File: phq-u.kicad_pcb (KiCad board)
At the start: 4 copper layers, 130.4 x 75.4 mm, 107 parts, among them J1 18…56 V, J2 MCU bypass, J3 Voltage select, J4 3.3…24 V, J5 MCU disable, J6 TC2030, J7 USB-C, J8 I/O, Q1 NX138AK, U1 i7A4W033A033V, U2 TMCS1108A1U, U3 TMCS1108A1U, U4 RPMH3.3-0.5, U5 ESP32-C3, U6 ECMF02-2AMX6

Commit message: Position mounting holes closer to corners
A distance of 7.5 mm to the edges should provide sufficient mechanical
stability.
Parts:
- moved H1 3.54 mm to (84.9, 69.7)
- moved H2 3.54 mm to (84.9, 130.1)
- moved H3 3.54 mm to (200.4, 69.7)
- moved H4 3.54 mm to (200.4, 130.1)
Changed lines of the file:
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@@
   )
   (footprint "MountingHole:MountingHole_3.2mm_M3_Pad_Via" (layer "F.Cu")
-    (at 87.44 72.2)
+    (at 84.94 69.7)
     (descr "Mounting Hole 3.2mm, M3")
     (tags "mounting hole 3.2mm m3")
@@
   )
   (footprint "MountingHole:MountingHole_3.2mm_M3_Pad_Via" (layer "F.Cu")
-    (at 197.87 72.2)
+    (at 200.37 69.7)
     (descr "Mounting Hole 3.2mm, M3")
     (tags "mounting hole 3.2mm m3")
@@
   )
   (footprint "MountingHole:MountingHole_3.2mm_M3_Pad_Via" (layer "F.Cu")
-    (at 197.87 127.6)
+    (at 200.37 130.1)
     (descr "Mounting Hole 3.2mm, M3")
     (tags "mounting hole 3.2mm m3")
@@
   )
   (footprint "MountingHole:MountingHole_3.2mm_M3_Pad_Via" (layer "F.Cu")
-    (at 87.44 127.6)
+    (at 84.94 130.1)
     (descr "Mounting Hole 3.2mm, M3")
     (tags "mounting hole 3.2mm m3")

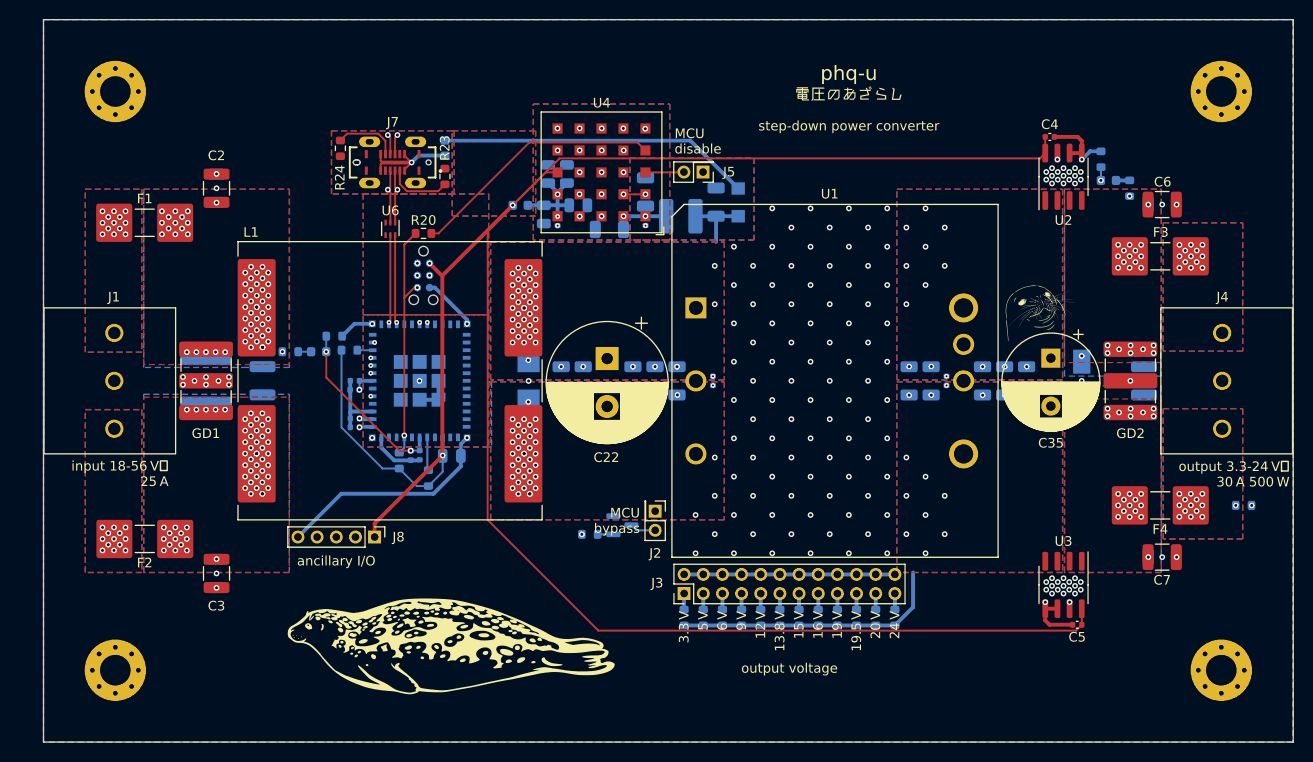
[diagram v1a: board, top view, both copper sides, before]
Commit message: Add 3.3 V TVS diodes and revise ground zones
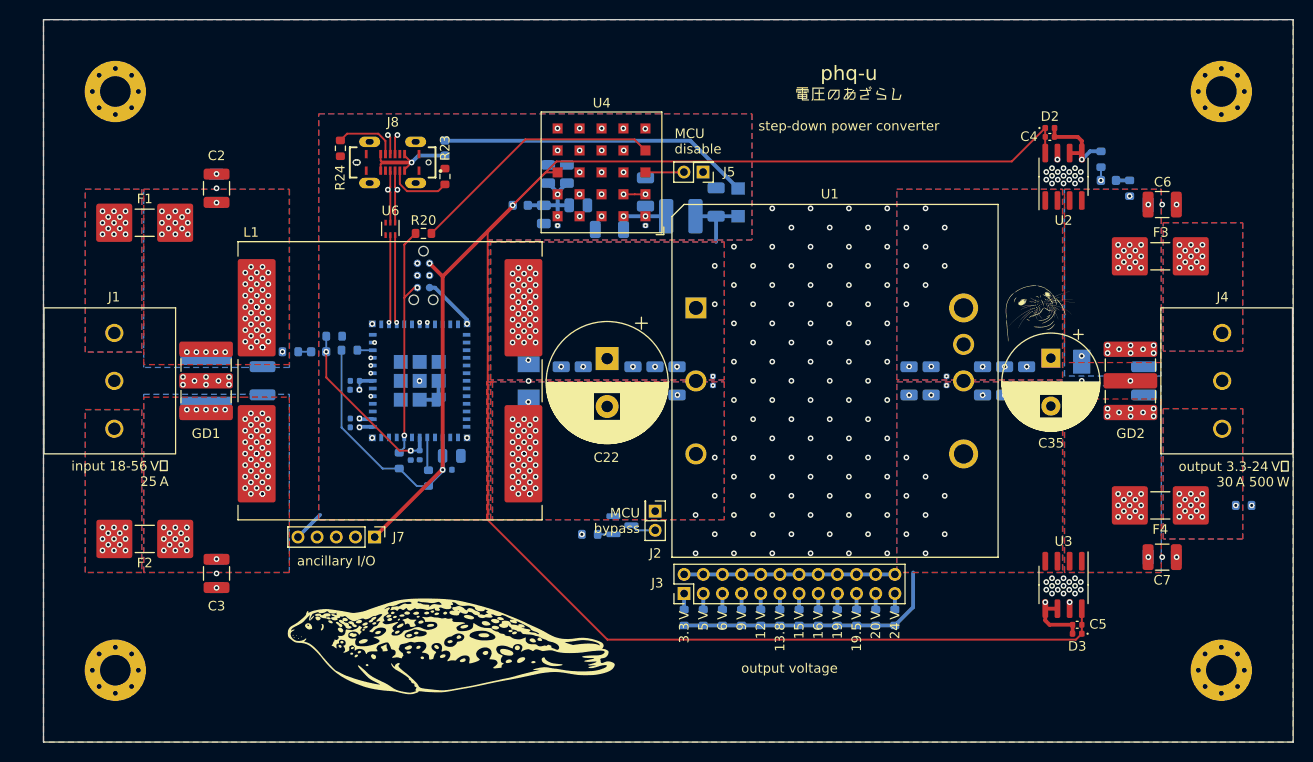
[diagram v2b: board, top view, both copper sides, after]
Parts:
- added D2: 3V3, Diode_SMD:D_0402_1005Metric, F.Cu at (182.5, 73.5)
- added D3: 3V3, Diode_SMD:D_0402_1005Metric, F.Cu at (185.3, 126.3)
- added D8: 3V3, Diode_SMD:D_0402_1005Metric, B.Cu at (119.6, 109.2)
- renumbered C15 to C14, C14 to C15, C18 to C16, C16 to C17, C17 to C18, D2 to D4, D3 to D5, D4 to D6, D5 to D7, J8 to J7, J7 to J8
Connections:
- C35 pad 2: (no net) -> GND
- C4 pad 1: (no net) -> GND
- C5 pad 2: (no net) -> GND
- R18 pad 2: (no net) -> GND
- U2 pad 5: (no net) -> GND
- U2 pad 6: (no net) -> GND
- U3 pad 5: (no net) -> GND
- U3 pad 6: (no net) -> GND
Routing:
- net GND: track 142.3 -> 108.2 mm
- net +3V3: track 236.3 -> 239.7 mm

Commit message: Correct clearance violations
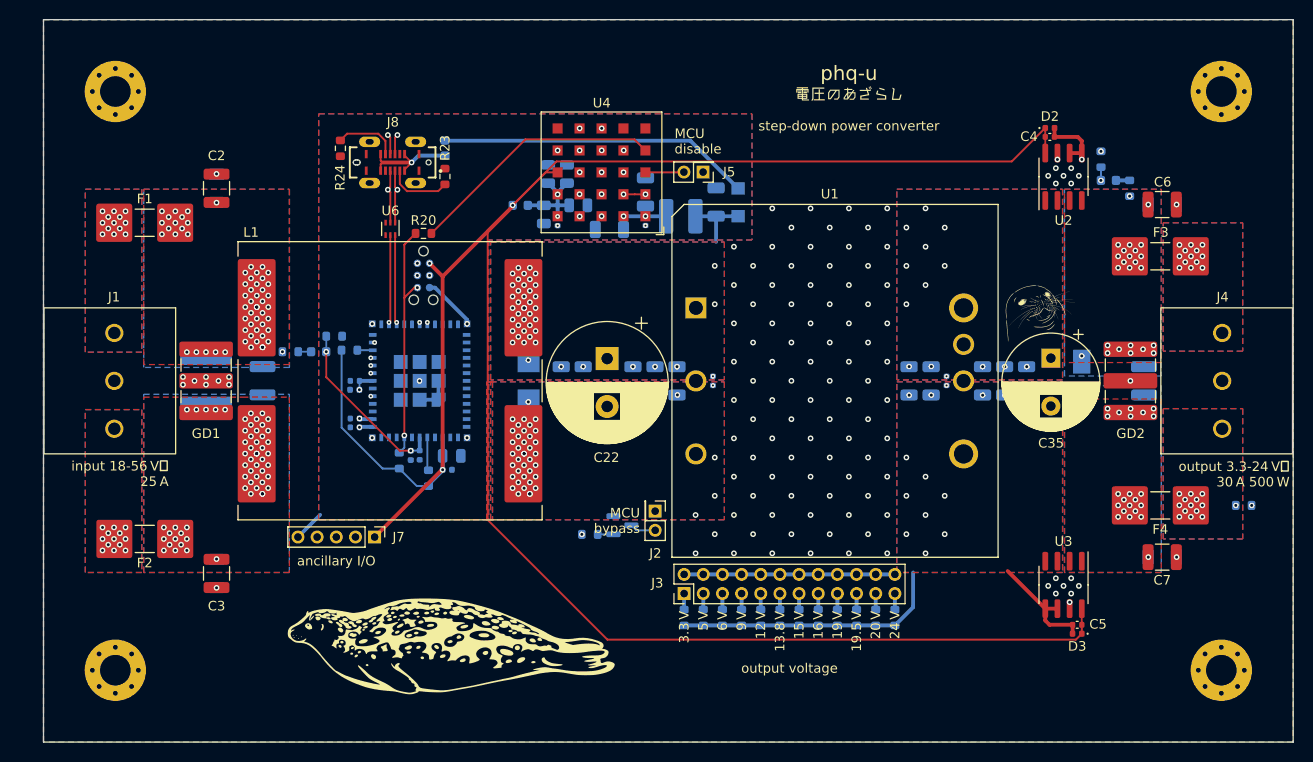
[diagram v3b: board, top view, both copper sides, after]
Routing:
- net GND: track 108.2 -> 94.9 mm
- net ESP_AD1_0: track 84.2 -> 83.4 mm
- net unconnected-(U4-PadE1): track 0.03 -> 0.00 mm, vias 1 -> 0
- net unconnected-(U4-PadE5): track 0.01 -> 0.00 mm, vias 1 -> 0
- net unconnected-(U4-PadE2): track 0.01 -> 0.00 mm, vias 1 -> 0
- net Earth: vias 134 -> 114
- net (no net): vias 6 -> 0

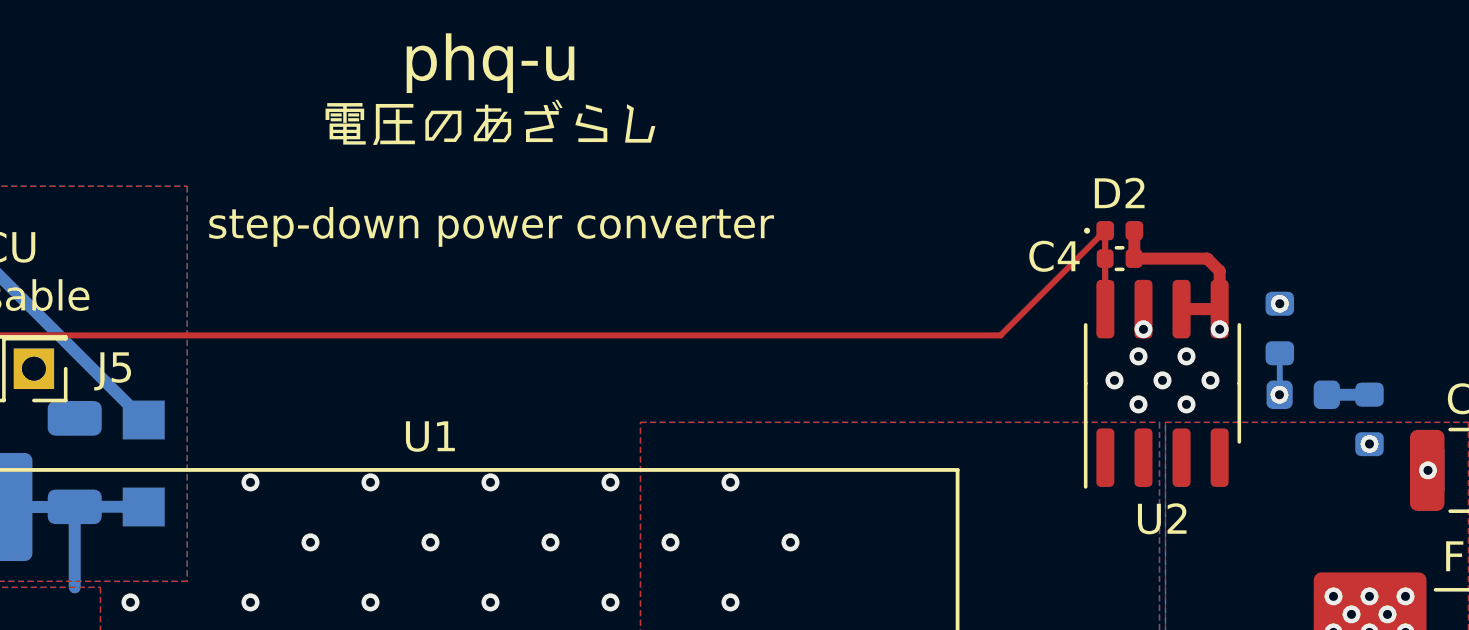
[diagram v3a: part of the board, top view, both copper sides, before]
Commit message: Re‐route ground traces
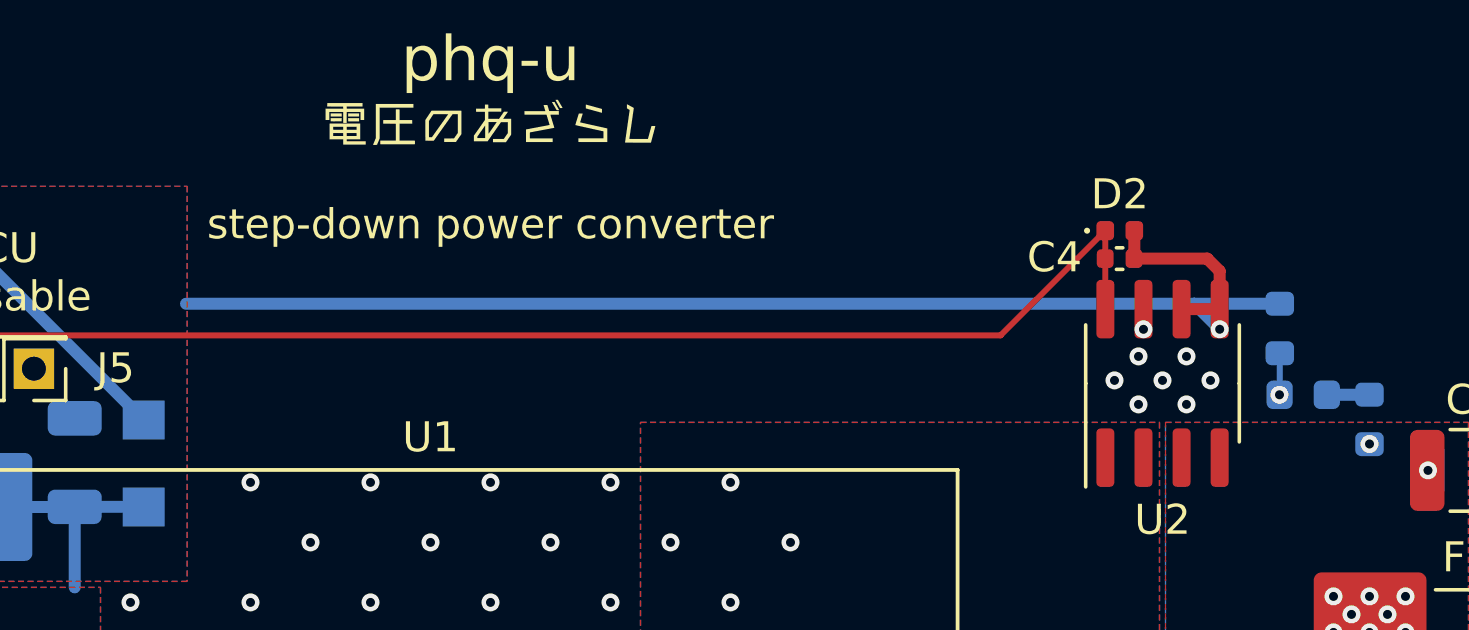
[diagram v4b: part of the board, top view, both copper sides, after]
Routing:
- net GND: track 94.9 -> 100.5 mm, vias 85 -> 84
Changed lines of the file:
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@@
   (segment (start 181.995 123.675) (end 183.265 123.675) (width 0.4) (layer "F.Cu") (net 5))
   (segment (start 184.85 125.36) (end 184.85 126.28) (width 0.4) (layer "F.Cu") (net 5))
-  (via micro (at 187.81 75.945) (size 0.6) (drill 0.3) (layers "F.Cu" "B.Cu") (remove_unused_layers) (net 5))
   (via micro (at 121.643042 105.845395) (size 0.6) (drill 0.3) (layers "F.Cu" "B.Cu") (remove_unused_layers) (keep_end_layers) (net 5))
   (via micro (at 121.65 93.95) (size 0.6) (drill 0.3) (layers "F.Cu" "B.Cu") (remove_unused_layers) (keep_end_layers) (net 5))
@@
   (via micro (at 127 109.3) (size 0.6) (drill 0.3) (layers "F.Cu" "B.Cu") (remove_unused_layers) (keep_end_layers) (net 5))
   (segment (start 185.80657 76.795739) (end 186.604652 76.795739) (width 0.4) (layer "In2.Cu") (net 5))
-  (segment (start 188.52 91.55) (end 183.979511 96.090489) (width 0.4) (layer "In2.Cu") (net 5))
-  (segment (start 183.979511 96.090489) (end 183.979511 101.132812) (width 0.4) (layer "In2.Cu") (net 5))
-  (segment (start 188.52 78.711087) (end 188.52 91.55) (width 0.4) (layer "In2.Cu") (net 5))
-  (segment (start 183.979511 101.132812) (end 182.58 102.532323) (width 0.4) (layer "In2.Cu") (net 5))
-  (segment (start 186.604652 76.795739) (end 188.52 78.711087) (width 0.4) (layer "In2.Cu") (net 5))
-  (segment (start 188.52 78.711087) (end 188.52 76.655) (width 0.4) (layer "In2.Cu") (net 5))
-  (segment (start 188.52 76.655) (end 187.81 75.945) (width 0.4) (layer "In2.Cu") (net 5))
   (segment (start 166.3 125.425) (end 168.2 123.525) (width 0.4) (layer "B.Cu") (net 5))
+  (segment (start 187.81 75.945) (end 184.955 75.945) (width 0.4) (layer "B.Cu") (net 5))
+  (segment (start 185.80657 76.795739) (end 185.805739 76.795739) (width 0.4) (layer "B.Cu") (net 5))
   (segment (start 144.3 125.425) (end 166.3 125.425) (width 0.4) (layer "B.Cu") (net 5))
   (segment (start 168.2 123.525) (end 168.2 119.9) (width 0.4) (layer "B.Cu") (net 5))
+  (segment (start 185.805739 76.795739) (end 184.955 75.945) (width 0.4) (layer "B.Cu") (net 5))
   (segment (start 117.735 90.17) (end 118.291493 90.17) (width 0.4) (layer "B.Cu") (net 5))
   (segment (start 118.291493 90.17) (end 121.65 93.528507) (width 0.4) (layer "B.Cu") (net 5))
+  (segment (start 184.955 75.945) (end 151.349881 75.945) (width 0.4) (layer "B.Cu") (net 5))
   (segment (start 118.675 99.9) (end 118.675 101.875) (width 0.4) (layer "B.Cu") (net 5))
   (segment (start 104 116.2) (end 106.31 113.89) (width 0.4) (layer "B.Cu") (net 5))
